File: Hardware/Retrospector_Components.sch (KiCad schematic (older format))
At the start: 145 parts, among them J1 SWD_Header, J2 Eurorack_10_pin_power, J3 Conn_01x08_Male, J4 Conn_01x08_Male, J5 Conn_01x08_Male, J6 Conn_01x08_Male, J7 USB_B_Micro, U1 STM32H743ZITx, U10 LM2675M-5, U11 TL072, U2 IS42S16800F-7TLI, U3 PCM5100APW, U4 SSI2164, U5 MCP6004, U6 MCP6004, U7 TL074, U8 LD1117-3.3-4Tab, Y1 8MHz 20pF

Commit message: Added some test code using SPI to control Toshiba LED controller
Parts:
- U4: value SSI2164 -> AS3364
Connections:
- net AUDIO_IN_L: now also U5.7; no longer U5.1
- net AUDIO_IN_R: now also U5.1; no longer U5.7
- net CLOCK: now also J4.1 (Pin_1); no longer J4.7 (Pin_7)
- net CLOCK_SCALED: now also U1.48 (PB2); no longer U1.127 (PG12)
- net DELAY_CV_SCALED_L: now also U1.42 (PA6); no longer U1.34 (PA0)
- net DELAY_CV_SCALED_R: now also U1.34 (PA0); no longer U1.42 (PA6)
- net FEEDBACK_CV: now also J4.7 (Pin_7); no longer J4.5 (Pin_5)
- net FEEDBACK_CV_SCALED: now also U6.14; no longer U6.7
- net FILTER_CV: now also J4.5 (Pin_5); no longer J4.1 (Pin_1)
- net FILTER_CV_SCALED: now also U6.1; no longer U6.14
- net GND: now also U5.3 (+), U5.5 (+), U6.12 (+), U6.2 (-), U6.5 (+); no longer U5.3 (+), U5.5 (+), U6.13 (-), U6.3 (+), U6.5 (+)
- net MIX_CV: now also J4.3 (Pin_3); no longer J4.2 (Pin_2)
- net MIX_POT: now also J4.2 (Pin_2); no longer J4.3 (Pin_3)
- net WET_DRY_MIX: now also U6.7; no longer U6.1
- net at C45.2, R11.2, R4.1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: now also U6.13 (-); no longer U6.6 (-)
- net at C29.2, R12.2, R6.1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: now also U5.6 (-); no longer U5.2 (-)
- net at C30.2, R13.2, R8.1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: now also U5.2 (-); no longer U5.6 (-)
- net at R29.1, R30.1, R31.1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: now also U6.6 (-); no longer U6.2 (-)
- net at C55.2, R35.1, R42.1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: now also U6.3 (+); no longer U6.12 (+)
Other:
- note added: "AS3364D (linear VCA) with R43 and C56 in place;\nRemove for SSI2164 (exponential)"
- note removed: "Can use AS3364D (linerar VCA) with R43 and C56 in place;\nRemove for SSI2164"
- moved on the sheet: TP1, TP10, TP11, TP12, TP2, TP3, TP4, TP5, TP6, TP7, TP8, TP9

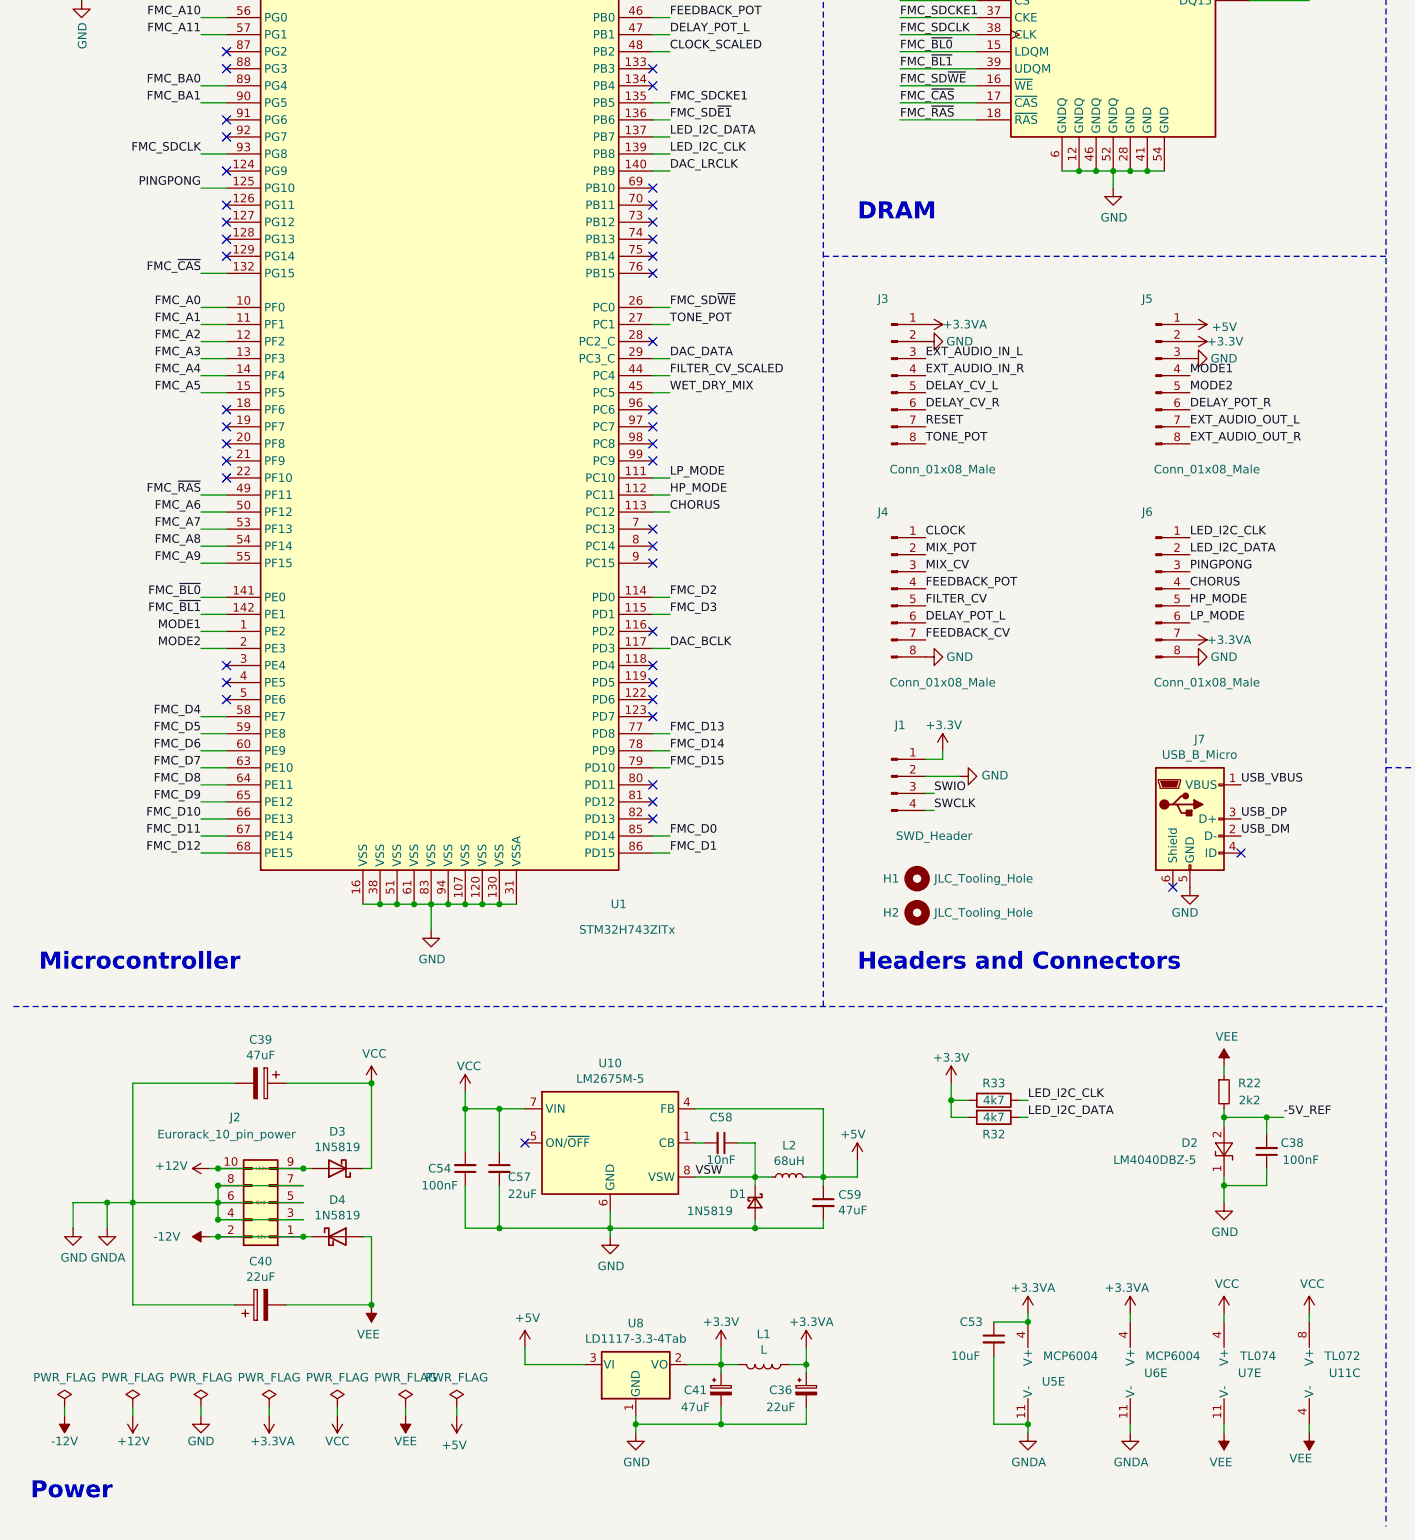
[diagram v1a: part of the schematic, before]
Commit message: Schematics updated for SPI LED Driver
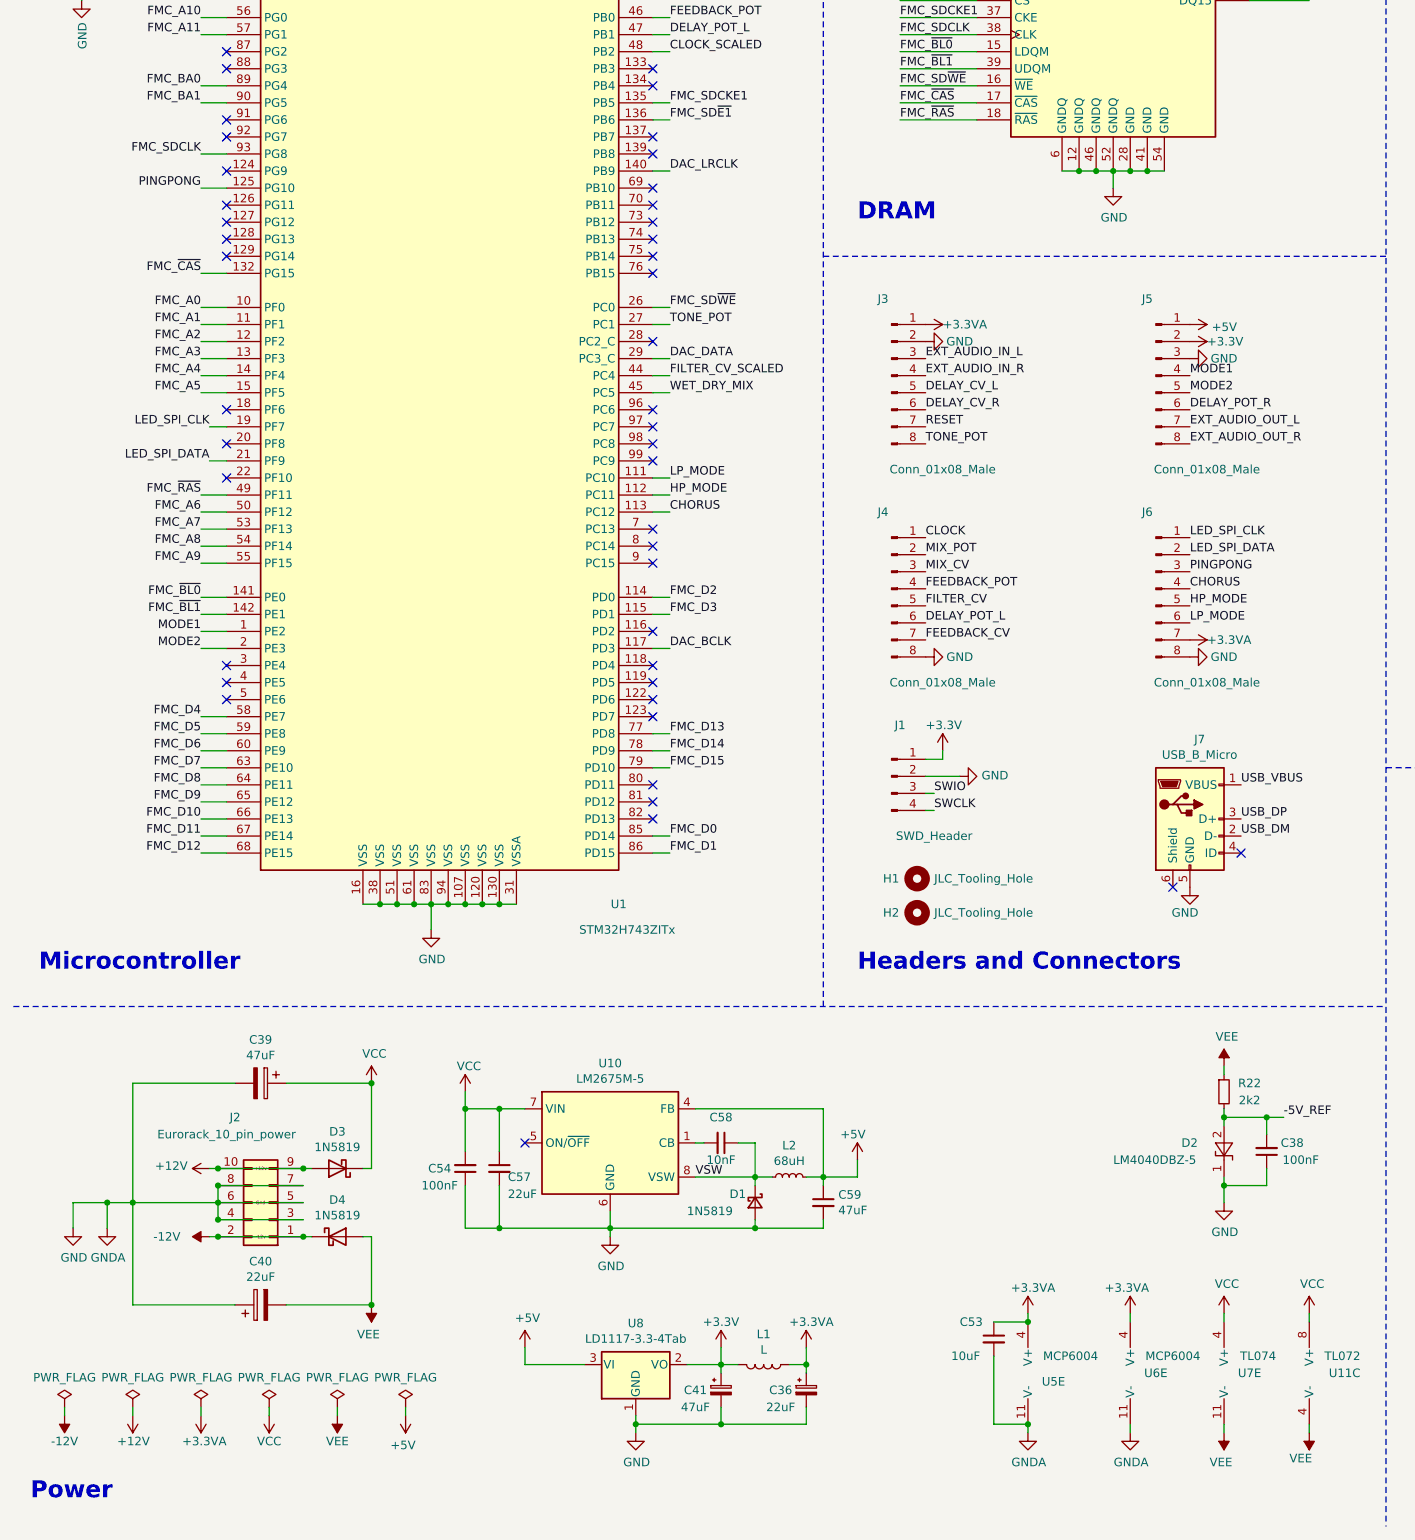
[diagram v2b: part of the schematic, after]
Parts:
- removed R32, R33: 4k7, Resistors_SMD:R_0603_HandSoldering, symbol Device:R
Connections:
- net LED_SPI_CLK: now reaches U1.19 (PF7)
- net LED_SPI_CLK: now also J6.1 (Pin_1)
- net LED_SPI_DATA: now reaches U1.21 (PF9)
- net LED_SPI_DATA: now also J6.2 (Pin_2)
- net LED_I2C_CLK: no longer names the net of U1.139 (PB8)
- net LED_I2C_CLK: no longer J6.1 (Pin_1)
- net LED_I2C_DATA: no longer names the net of U1.137 (PB7)
- net LED_I2C_DATA: no longer J6.2 (Pin_2)
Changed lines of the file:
@@
 $EndComp
 $Comp
-L power:PWR_FLAG #FLG05
-U 1 1 5C368914
-P 1600 11800
-F 0 "#FLG05" H 1600 11875 50  0001 C CNN
-F 1 "PWR_FLAG" H 1600 11974 50  0000 C CNN
-F 2 "" H 1600 11800 50  0001 C CNN
-F 3 "~" H 1600 11800 50  0001 C CNN
-	1    1600 11800
-	1    0    0    -1
-$EndComp
-$Comp
-L power:GND #PWR089
-U 1 1 5C368939
-P 1600 11850
-F 0 "#PWR089" H 1600 11600 50  0001 C CNN
-F 1 "GND" H 1600 11700 50  0000 C CNN
-F 2 "" H 1600 11850 50  0001 C CNN
-F 3 "" H 1600 11850 50  0001 C CNN
-	1    1600 11850
-	1    0    0    -1
-$EndComp
-Wire Wire Line
-	1600 11800 1600 11850
-$Comp
 L Amplifier_Operational:MCP6004 U5
 U 3 1 5C61BC1D
@@
 L power:PWR_FLAG #FLG02
 U 1 1 5CB20466
-P 2000 11800
-F 0 "#FLG02" H 2000 11875 50  0001 C CNN
-F 1 "PWR_FLAG" H 2000 11974 50  0000 C CNN
-F 2 "" H 2000 11800 50  0001 C CNN
-F 3 "~" H 2000 11800 50  0001 C CNN
-	1    2000 11800
+P 1600 11800
+F 0 "#FLG02" H 1600 11875 50  0001 C CNN
+F 1 "PWR_FLAG" H 1600 11974 50  0000 C CNN
+F 2 "" H 1600 11800 50  0001 C CNN
+F 3 "~" H 1600 11800 50  0001 C CNN
+	1    1600 11800
 	1    0    0    -1
 $EndComp
 Wire Wire Line
-	2000 11800 2000 11850
+	1600 11800 1600 11850
 $Comp
 L power:+3.3VA #PWR084
 U 1 1 5CB34D3A
-P 2000 11850
-F 0 "#PWR084" H 2000 11700 50  0001 C CNN
-F 1 "+3.3VA" H 1850 12000 50  0000 L CNN
-F 2 "" H 2000 11850 50  0001 C CNN
-F 3 "" H 2000 11850 50  0001 C CNN
-	1    2000 11850
+P 1600 11850
+F 0 "#PWR084" H 1600 11700 50  0001 C CNN
+F 1 "+3.3VA" H 1450 12000 50  0000 L CNN
+F 2 "" H 1600 11850 50  0001 C CNN
+F 3 "" H 1600 11850 50  0001 C CNN
+	1    1600 11850
 	-1   0    0    1
 $EndComp
@@
 L power:VEE #PWR090
 U 1 1 5CB35B68
-P 2800 11850
-F 0 "#PWR090" H 2800 11700 50  0001 C CNN
-F 1 "VEE" H 2800 12000 50  0000 C CNN
-F 2 "" H 2800 11850 50  0001 C CNN
-F 3 "" H 2800 11850 50  0001 C CNN
-	1    2800 11850
+P 2400 11850
+F 0 "#PWR090" H 2400 11700 50  0001 C CNN
+F 1 "VEE" H 2400 12000 50  0000 C CNN
+F 2 "" H 2400 11850 50  0001 C CNN
+F 3 "" H 2400 11850 50  0001 C CNN
+	1    2400 11850
 	-1   0    0    1
 $EndComp
@@
 $EndComp
 Wire Wire Line
-	2800 11800 2800 11850
+	2400 11800 2400 11850
 $Comp
 L power:PWR_FLAG #FLG06
 U 1 1 5CB4D472
-P 2800 11800
-F 0 "#FLG06" H 2800 11875 50  0001 C CNN
-F 1 "PWR_FLAG" H 2800 11974 50  0000 C CNN
-F 2 "" H 2800 11800 50  0001 C CNN
-F 3 "~" H 2800 11800 50  0001 C CNN
-	1    2800 11800
+P 2400 11800
+F 0 "#FLG06" H 2400 11875 50  0001 C CNN
+F 1 "PWR_FLAG" H 2400 11974 50  0000 C CNN
+F 2 "" H 2400 11800 50  0001 C CNN
+F 3 "~" H 2400 11800 50  0001 C CNN
+	1    2400 11800
 	1    0    0    -1
 $EndComp
 Wire Wire Line
-	2400 11800 2400 11850
+	2000 11800 2000 11850
 $Comp
 L power:PWR_FLAG #FLG03
 U 1 1 5CB61F63
-P 2400 11800
-F 0 "#FLG03" H 2400 11875 50  0001 C CNN
-F 1 "PWR_FLAG" H 2400 11974 50  0000 C CNN
-F 2 "" H 2400 11800 50  0001 C CNN
-F 3 "~" H 2400 11800 50  0001 C CNN
-	1    2400 11800
+P 2000 11800
+F 0 "#FLG03" H 2000 11875 50  0001 C CNN
+F 1 "PWR_FLAG" H 2000 11974 50  0000 C CNN
+F 2 "" H 2000 11800 50  0001 C CNN
+F 3 "~" H 2000 11800 50  0001 C CNN
+	1    2000 11800
 	1    0    0    -1
 $EndComp
@@
 L power:VCC #PWR085
 U 1 1 5CB7826E
-P 2400 11850
-F 0 "#PWR085" H 2400 11700 50  0001 C CNN
-F 1 "VCC" H 2400 12000 50  0000 C CNN
-F 2 "" H 2400 11850 50  0001 C CNN
-F 3 "" H 2400 11850 50  0001 C CNN
-	1    2400 11850
+P 2000 11850
+F 0 "#PWR085" H 2000 11700 50  0001 C CNN
+F 1 "VCC" H 2000 12000 50  0000 C CNN
+F 2 "" H 2000 11850 50  0001 C CNN
+F 3 "" H 2000 11850 50  0001 C CNN
+	1    2000 11850
 	-1   0    0    1
 $EndComp
@@
 NoConn ~ 1750 5050
 NoConn ~ 1750 5950
-NoConn ~ 1750 6050
 NoConn ~ 1750 6150
-NoConn ~ 1750 6250
 NoConn ~ 1750 6350
 NoConn ~ 1750 7450
@@
 	0    1    1    0
 $EndComp
-$Comp
-L Device:R R32
-U 1 1 5FE3B49C
-P 6250 10100
-F 0 "R32" V 6350 10100 50  0000 C CNN
-F 1 "4k7" V 6250 10100 50  0000 C CNN
-F 2 "Resistors_SMD:R_0603_HandSoldering" V 6180 10100 50  0001 C CNN
-F 3 "~" H 6250 10100 50  0001 C CNN
-F 4 "C23138" H 6250 10100 50  0001 C CNN "Part_Number"
-	1    6250 10100
-	0    1    1    0
-$EndComp
-$Comp
-L Device:R R33
-U 1 1 5FEA3045
-P 6250 10000
-F 0 "R33" V 6150 10000 50  0000 C CNN
-F 1 "4k7" V 6250 10000 50  0000 C CNN
-F 2 "Resistors_SMD:R_0603_HandSoldering" V 6180 10000 50  0001 C CNN
-F 3 "~" H 6250 10000 50  0001 C CNN
-F 4 "C23138" H 6250 10000 50  0001 C CNN "Part_Number"
-	1    6250 10000
-	0    1    1    0
-$EndComp
 Text Label 5850 6150 0    50   ~ 0
 TONE_POT
@@
 HP_MODE
 Text Label 7400 6700 0    50   ~ 0
-LED_I2C_CLK
+LED_SPI_CLK
 Text Label 7400 6800 0    50   ~ 0
-LED_I2C_DATA
+LED_SPI_DATA
 $Comp
 L power:+3.3V #PWR0126
@@
 	0    1    1    0
 $EndComp
-Text Label 4350 4450 0    50   ~ 0
-LED_I2C_CLK
-Text Label 4350 4350 0    50   ~ 0
-LED_I2C_DATA
+Text Label 1650 6050 2    50   ~ 0
+LED_SPI_CLK
+Text Label 1650 6250 2    50   ~ 0
+LED_SPI_DATA
 Wire Wire Line
-	4250 4350 4350 4350
+	1750 6250 1650 6250
 Wire Wire Line
-	4250 4450 4350 4450
+	1750 6050 1650 6050
 Text Label 5850 7100 0    50   ~ 0
 FILTER_CV
@@
 	0    -1   -1   0
 $EndComp
-Text Label 6450 10000 0    50   ~ 0
-LED_I2C_CLK
-Text Label 6450 10100 0    50   ~ 0
-LED_I2C_DATA
-Wire Wire Line
-	6400 10000 6450 10000
-$Comp
-L power:+3.3V #PWR0130
-U 1 1 60D9E779
-P 6000 9900
-F 0 "#PWR0130" H 6000 9750 50  0001 C CNN
-F 1 "+3.3V" H 6000 10050 50  0000 C CNN
-F 2 "" H 6000 9900 50  0001 C CNN
-F 3 "" H 6000 9900 50  0001 C CNN
-	1    6000 9900
-	1    0    0    -1
-$EndComp
-Wire Wire Line
-	6400 10100 6450 10100
-Wire Wire Line
-	6100 10000 6000 10000
-Wire Wire Line
-	6000 10000 6000 9900
-Wire Wire Line
-	6100 10100 6000 10100
-Wire Wire Line
-	6000 10100 6000 10000
-Connection ~ 6000 10000
 Wire Wire Line
 	5450 10350 5450 10450
@@
 L power:+5V #PWR0134
 U 1 1 6075A433
-P 3100 11850
-F 0 "#PWR0134" H 3100 11700 50  0001 C CNN
-F 1 "+5V" H 3115 12023 50  0000 C CNN
-F 2 "" H 3100 11850 50  0001 C CNN
-F 3 "" H 3100 11850 50  0001 C CNN
-	1    3100 11850
+P 2800 11850
+F 0 "#PWR0134" H 2800 11700 50  0001 C CNN
+F 1 "+5V" H 2815 12023 50  0000 C CNN
+F 2 "" H 2800 11850 50  0001 C CNN
+F 3 "" H 2800 11850 50  0001 C CNN
+	1    2800 11850
 	-1   0    0    1
 $EndComp
 Wire Wire Line
-	3100 11850 3100 11800
+	2800 11850 2800 11800
 $Comp
 L Connector:USB_B_Micro J7
@@
 L power:PWR_FLAG #FLG0101
 U 1 1 60B14DA2
-P 3100 11800
-F 0 "#FLG0101" H 3100 11875 50  0001 C CNN
-F 1 "PWR_FLAG" H 3100 11974 50  0000 C CNN
-F 2 "" H 3100 11800 50  0001 C CNN
-F 3 "~" H 3100 11800 50  0001 C CNN
-	1    3100 11800
+P 2800 11800
+F 0 "#FLG0101" H 2800 11875 50  0001 C CNN
+F 1 "PWR_FLAG" H 2800 11974 50  0000 C CNN
+F 2 "" H 2800 11800 50  0001 C CNN
+F 3 "~" H 2800 11800 50  0001 C CNN
+	1    2800 11800
 	1    0    0    -1
 $EndComp
@@
 $EndComp
 NoConn ~ 1750 4850
+NoConn ~ 4250 4350
+NoConn ~ 4250 4450
 $EndSCHEMATC

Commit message: Work on PCB routing
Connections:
- net AUDIO_IN_L: now also U1.37 (PA3); no longer U1.36 (PA2)
- net AUDIO_IN_R: now also U1.36 (PA2); no longer U1.37 (PA3)
- net DELAY_CV_L: now also J3.3 (Pin_3); no longer J3.5 (Pin_5)
- net DELAY_CV_R: now also J3.4 (Pin_4); no longer J3.6 (Pin_6)
- net DELAY_POT_R: now also J3.7 (Pin_7); no longer J5.6 (Pin_6)
- net EXT_AUDIO_IN_L: now also J3.5 (Pin_5); no longer J3.3 (Pin_3)
- net EXT_AUDIO_IN_R: now also J3.6 (Pin_6); no longer J3.4 (Pin_4)
- net LED_SPI_CLK: now also J6.2 (Pin_2), U1.128 (PG13); no longer J6.1 (Pin_1), U1.19 (PF7)
- net LED_SPI_DATA: now also J6.1 (Pin_1), U1.129 (PG14); no longer J6.2 (Pin_2), U1.21 (PF9)
- net RESET: now also J5.6 (Pin_6); no longer J3.7 (Pin_7)
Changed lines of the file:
@@
 NoConn ~ 1750 4250
 NoConn ~ 1750 4350
-NoConn ~ 1750 4950
-NoConn ~ 1750 5050
 NoConn ~ 1750 5950
 NoConn ~ 1750 6150
@@
 Text Label 10450 1950 0    50   ~ 0
 AUDIO_IN_L
-Text Label 5850 5750 0    50   ~ 0
+Text Label 5850 5950 0    50   ~ 0
 EXT_AUDIO_IN_R
-Text Label 5850 5650 0    50   ~ 0
+Text Label 5850 5850 0    50   ~ 0
 EXT_AUDIO_IN_L
 Text Label 7400 6150 0    50   ~ 0
@@
 Wire Wire Line
 	1650 1950 1750 1950
-Text Label 5850 6050 0    50   ~ 0
+Text Label 7400 5950 0    50   ~ 0
 RESET
-Text Label 5850 5850 0    50   ~ 0
+Text Label 5850 5650 0    50   ~ 0
 DELAY_CV_L
-Text Label 5850 5950 0    50   ~ 0
+Text Label 5850 5750 0    50   ~ 0
 DELAY_CV_R
 Text Label 5850 7300 0    50   ~ 0
@@
 Text Label 4350 2550 0    50   ~ 0
 DELAY_CV_SCALED_L
-Text Label 4350 2150 0    50   ~ 0
-AUDIO_IN_L
 Text Label 4350 2250 0    50   ~ 0
+AUDIO_IN_L
+Text Label 4350 2150 0    50   ~ 0
 AUDIO_IN_R
 Text Label 4350 3750 0    50   ~ 0
@@
 Text Label 7400 7100 0    50   ~ 0
 HP_MODE
-Text Label 7400 6700 0    50   ~ 0
-LED_SPI_CLK
 Text Label 7400 6800 0    50   ~ 0
+LED_SPI_CLK
+Text Label 7400 6700 0    50   ~ 0
 LED_SPI_DATA
 $Comp
@@
 	0    1    1    0
 $EndComp
-Text Label 1650 6050 2    50   ~ 0
+Text Label 1600 4950 2    50   ~ 0
 LED_SPI_CLK
-Text Label 1650 6250 2    50   ~ 0
+Text Label 1600 5050 2    50   ~ 0
 LED_SPI_DATA
-Wire Wire Line
-	1750 6250 1650 6250
-Wire Wire Line
-	1750 6050 1650 6050
 Text Label 5850 7100 0    50   ~ 0
 FILTER_CV
@@
 Text Label 7400 5750 0    50   ~ 0
 MODE1
-Text Label 7400 5950 0    50   ~ 0
+Text Label 5850 6050 0    50   ~ 0
 DELAY_POT_R
 NoConn ~ 1750 4550
@@
 NoConn ~ 4250 4350
 NoConn ~ 4250 4450
+Wire Wire Line
+	1600 4950 1750 4950
+Wire Wire Line
+	1600 5050 1750 5050
+NoConn ~ 1750 6050
+NoConn ~ 1750 6250
 $EndSCHEMATC
